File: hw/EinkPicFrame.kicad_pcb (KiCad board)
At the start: 2 copper layers, 0 parts

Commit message: HW: Created PCB
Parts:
- added C1: 100 nF, Capacitor_THT:C_Disc_D5.1mm_W3.2mm_P5.00mm, F.Cu at (115.0, 103.5)
- added C2: 0.1 uF, Capacitor_THT:C_Disc_D5.1mm_W3.2mm_P5.00mm, F.Cu at (132.2, 103.8)
- added C3: CP, Capacitor_THT:CP_Radial_D6.3mm_P2.50mm, F.Cu at (103.0, 95.8)
- added C4: 0.1 uF, Capacitor_THT:C_Disc_D5.1mm_W3.2mm_P5.00mm, F.Cu at (137.2, 89.8)
- added D1: LED, LED_THT:LED_D4.0mm, F.Cu at (103.6, 101.3)
- added J1: SD, Connector_PinSocket_2.54mm:PinSocket_1x06_P2.54mm_Vertical, F.Cu at (176.5, 103.0)
- added J2: AVR-ISP-6, Connector_PinHeader_2.54mm:PinHeader_2x03_P2.54mm_Vertical, F.Cu at (156.0, 94.0)
- added J3: EPD, Connector_PinHeader_2.54mm:PinHeader_2x04_P2.54mm_Vertical, F.Cu at (172.5, 98.0)
- added J4: Power, Connector_PinHeader_2.54mm:PinHeader_1x02_P2.54mm_Vertical, F.Cu at (105.5, 89.5)
- added J5: UART, Connector_PinSocket_2.54mm:PinSocket_1x03_P2.54mm_Vertical, F.Cu at (127.8, 103.8)
- added J6: TRIG, Connector_PinHeader_2.54mm:PinHeader_1x02_P2.54mm_Vertical, F.Cu at (111.2, 89.5)
- added Q1: 2N7000, Package_TO_SOT_THT:TO-92_Inline, F.Cu at (163.0, 103.0)
- added Q2: 2N7000, Package_TO_SOT_THT:TO-92_Inline, F.Cu at (163.0, 90.8)
- added R1: 1M, Resistor_THT:R_Axial_DIN0204_L3.6mm_D1.6mm_P2.54mm_Vertical, F.Cu at (172.5, 101.2)
- added R10: 1M, Resistor_THT:R_Axial_DIN0204_L3.6mm_D1.6mm_P2.54mm_Vertical, F.Cu at (141.2, 103.8)
- added R11: 330, Resistor_THT:R_Axial_DIN0204_L3.6mm_D1.6mm_P2.54mm_Vertical, F.Cu at (107.6, 103.5)
- added R2: 10K, Resistor_THT:R_Axial_DIN0204_L3.6mm_D1.6mm_P2.54mm_Vertical, F.Cu at (118.2, 103.0)
- added R3: 1M, Resistor_THT:R_Axial_DIN0204_L3.6mm_D1.6mm_P2.54mm_Vertical, F.Cu at (170.0, 101.2)
- added R4: 330, Resistor_THT:R_Axial_DIN0204_L3.6mm_D1.6mm_P2.54mm_Vertical, F.Cu at (162.5, 96.5)
- added R5: 330, Resistor_THT:R_Axial_DIN0204_L3.6mm_D1.6mm_P2.54mm_Vertical, F.Cu at (162.5, 94.0)
- added R6: 330, Resistor_THT:R_Axial_DIN0204_L3.6mm_D1.6mm_P2.54mm_Vertical, F.Cu at (162.5, 99.0)
- added R7: 180, Resistor_THT:R_Axial_DIN0204_L3.6mm_D1.6mm_P2.54mm_Vertical, F.Cu at (158.5, 103.0)
- added R8: 180, Resistor_THT:R_Axial_DIN0204_L3.6mm_D1.6mm_P2.54mm_Vertical, F.Cu at (158.5, 90.8)
- added R9: 1M, Resistor_THT:R_Axial_DIN0204_L3.6mm_D1.6mm_P2.54mm_Vertical, F.Cu at (148.8, 103.8)
- added REF**: KiCad-Logo2_5mm_SilkScreen, Symbol:KiCad-Logo2_5mm_SilkScreen, B.Cu at (134.7, 96.9)
- added SW1: SW_Push, Button_Switch_THT:SW_PUSH_6mm, F.Cu at (110.2, 100.0)
- added U1: ATmega328P-PU, Package_DIP:DIP-28_W7.62mm, F.Cu at (118.2, 100.5)
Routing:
- net +3V3: track 0.00 -> 232.6 mm
- net RESET: track 0.00 -> 55.3 mm
- net SDCS: track 0.00 -> 51.3 mm
- net DPCS: track 0.00 -> 31.7 mm
- net SDFET: track 0.00 -> 29.6 mm
- net LED: track 0.00 -> 26.5 mm
- net DPRST: track 0.00 -> 26.4 mm
- net DPBUSY: track 0.00 -> 25.4 mm
- net Net-(J2-Pad3): track 0.00 -> 23.9 mm
- net TRIG: track 0.00 -> 23.4 mm
- net Net-(J2-Pad1): track 0.00 -> 21.3 mm
- net DPDC: track 0.00 -> 20.5 mm
- net Net-(J2-Pad4): track 0.00 -> 17.8 mm
- net SCK: track 0.00 -> 14.5 mm
- net DPFET: track 0.00 -> 13.6 mm
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- added copper zone on B.Cu, net GND
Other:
- board outline added: 80 x 21.6 mm
- net class Power added: clearance 0.2, trace_width 0.5, via_dia 0.8, via_drill 0.4
- board text added: "(c) haJu 2022"
- board text added: "BSY"
- board text added: "CS"
- board text added: "DC"
- board text added: "EInkPicFrame 1.0"
- board text added: "GND"
- board text added: "IN"
- board text added: "ISP GND"
- board text added: "MISO"
- board text added: "MOSI"
- board text added: "RST"
- board text added: "RX"
- board text added: "Reset"
- board text added: "SCK"
- board text added: "TRIG"
- board text added: "TX"
- board text added: "VCC"

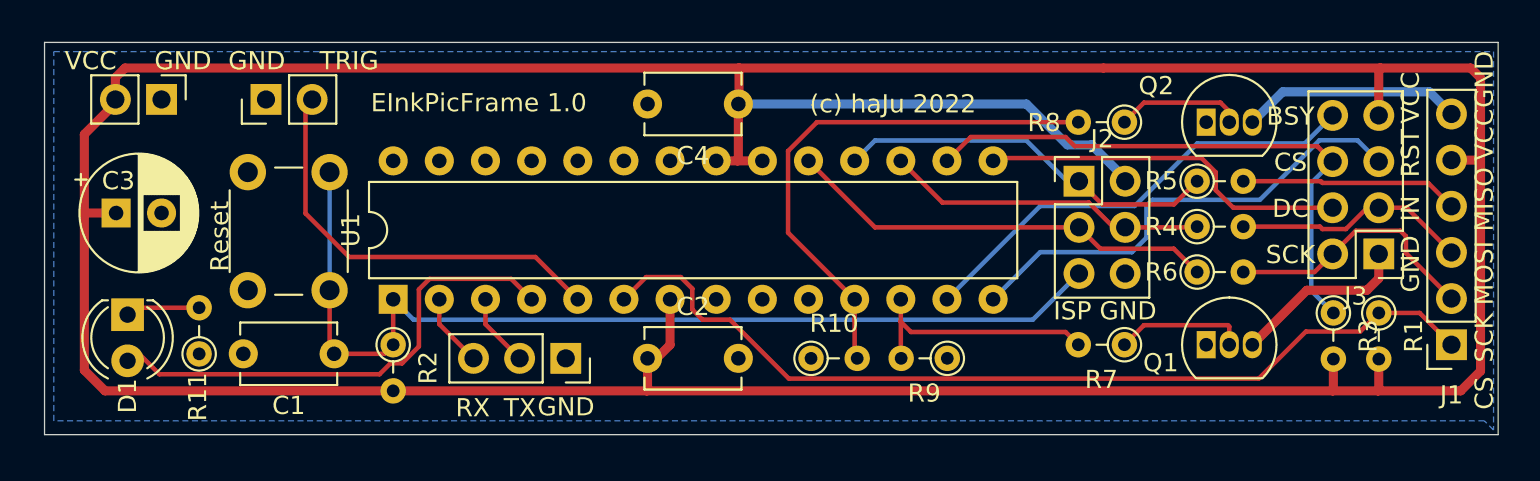
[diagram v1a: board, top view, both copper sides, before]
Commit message: HW: Added possibility to add a crystal
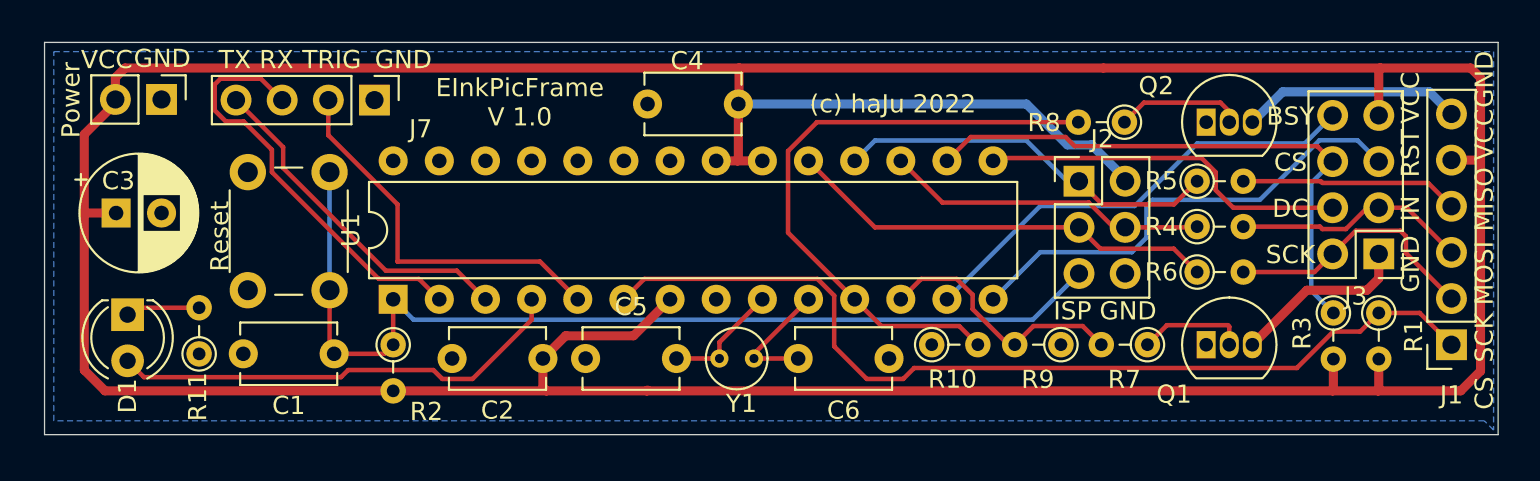
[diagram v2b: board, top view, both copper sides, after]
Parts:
- removed J5: UART, Connector_PinSocket_2.54mm:PinSocket_1x03_P2.54mm_Vertical
- removed J6: TRIG, Connector_PinHeader_2.54mm:PinHeader_1x02_P2.54mm_Vertical
- added C5: 22 pF, Capacitor_THT:C_Disc_D5.1mm_W3.2mm_P5.00mm, F.Cu at (128.8, 103.8)
- added C6: 22 pF, Capacitor_THT:C_Disc_D5.1mm_W3.2mm_P5.00mm, F.Cu at (145.5, 103.8)
- added J7: Debug, Connector_PinHeader_2.54mm:PinHeader_1x04_P2.54mm_Vertical, F.Cu at (117.2, 89.5)
- added Y1: Crystal, Crystal:Crystal_C38-LF_D3.0mm_L8.0mm_Vertical, F.Cu at (136.2, 103.8)
- moved R10 6.68 mm to (147.9, 103.0)
- moved R9 6.30 mm to (155.0, 103.0)
- moved C2 5.76 mm to (126.5, 103.8), turned to 180 degrees
- moved R7 1.27 mm to (159.8, 103.0)
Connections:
- U1 pad 10: Net-(U1-Pad10) -> XTAL2
- U1 pad 9: Net-(U1-Pad9) -> XTAL1
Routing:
- net RXD: track 4.03 -> 23.1 mm
- net TXD: track 4.03 -> 18.9 mm
- net XTAL2: track 0.00 -> 7.25 mm
- net XTAL1: track 0.00 -> 6.60 mm
- net SDFET: track 29.6 -> 34.1 mm
- net +3V3: track 232.6 -> 237.0 mm
- net TRIG: track 23.4 -> 21.2 mm
- net Net-(Q1-Pad2): track 7.25 -> 5.98 mm
- net LED: track 26.5 -> 25.5 mm
- net SDCS: track 51.3 -> 52.2 mm
- net DPFET: track 13.6 -> 14.3 mm
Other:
- board text added: "EInkPicFrame V 1.0"
- board text added: "Power"
- board text removed: "EInkPicFrame 1.0"

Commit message: HW: ADC + Small improvements (V1.1)
Added proper wiring for AVCC and AREF according to data sheet
 * 100 nF capacitor to ground on AREF
 *  10 uH inductor on AVCC

 Added header for unused PortC pins
  * May be used as 2nd SPI (bit bang)
  * Independent SPI would allow to power EPD and SD independently

Use larger footprint for the FET transistors for easier soldering

Add a jumper to disconnect VCC without pulling battery connector
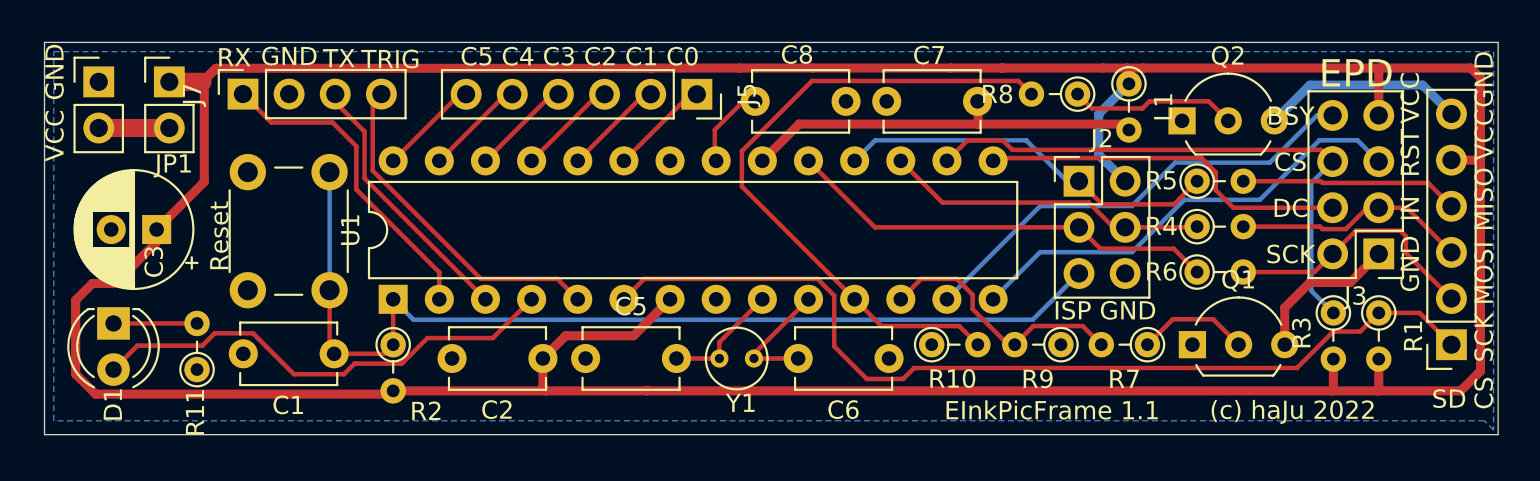
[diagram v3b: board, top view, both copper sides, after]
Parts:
- removed C4: 0.1 uF, Capacitor_THT:C_Disc_D5.1mm_W3.2mm_P5.00mm
- added C7: 0.1 uF, Capacitor_THT:C_Disc_D5.1mm_W3.2mm_P5.00mm, F.Cu at (145.4, 89.6)
- added C8: 0.1 uF, Capacitor_THT:C_Disc_D5.1mm_W3.2mm_P5.00mm, F.Cu at (138.2, 89.6)
- added J5: PORTC, Connector_PinSocket_2.54mm:PinSocket_1x06_P2.54mm_Vertical, F.Cu at (135.0, 89.2)
- added JP1: Jumper, Connector_PinHeader_2.54mm:PinHeader_1x02_P2.54mm_Vertical, F.Cu at (105.9, 88.5)
- added L1: 10 uH, Resistor_THT:R_Axial_DIN0204_L3.6mm_D1.6mm_P2.54mm_Vertical, F.Cu at (158.7, 88.6)
- J7: footprint Connector_PinHeader_2.54mm:PinHeader_1x04_P2.54mm_Vertical -> Connector_PinSocket_2.54mm:PinSocket_1x04_P2.54mm_Vertical
- Q1: footprint Package_TO_SOT_THT:TO-92_Inline -> Package_TO_SOT_THT:TO-92L_Inline_Wide
- Q2: footprint Package_TO_SOT_THT:TO-92_Inline -> Package_TO_SOT_THT:TO-92_Inline_Wide
- moved J7 7.25 mm to (110.0, 89.2), turned to 90 degrees
- moved J4 3.59 mm to (102.0, 88.5), turned to 0 degrees
- moved R8 3.00 mm to (155.9, 89.2)
- moved C3 2.41 mm to (105.2, 96.7), turned to 180 degrees
- moved Q2 1.33 mm to (161.7, 90.7)
- moved D1 0.91 mm to (102.9, 101.8)
- moved R11 0.87 mm to (107.5, 104.4)
- moved Q1 0.76 mm to (162.2, 103.0)
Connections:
- J4 pad 2: +3V3 -> Net-(J4-Pad2)
- J7 pad 1: GND -> RXD
- J7 pad 2: TRIG -> GND
- J7 pad 3: RXD -> TXD
- J7 pad 4: TXD -> TRIG
- U1 pad 20: +3V3 -> Net-(C7-Pad2)
- U1 pad 21: +3V3 -> Net-(C8-Pad1)
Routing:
- net Net-(C7-Pad2): track 0.00 -> 22.4 mm
- net +3V3: track 237.0 -> 215.1 mm
- net Net-(J5-Pad2): track 0.00 -> 5.53 mm
- net Net-(J5-Pad1): track 0.00 -> 5.53 mm
- net Net-(J5-Pad5): track 0.00 -> 5.53 mm
- net Net-(J5-Pad4): track 0.00 -> 5.53 mm
- net Net-(J5-Pad3): track 0.00 -> 5.53 mm
- net RXD: track 23.1 -> 17.7 mm
- net Net-(J5-Pad6): track 0.00 -> 5.10 mm
- net Net-(C8-Pad1): track 0.00 -> 4.54 mm
- net TXD: track 18.9 -> 14.9 mm
- net Net-(J4-Pad2): track 0.00 -> 3.89 mm
- net TRIG: track 21.2 -> 18.4 mm
- net SDFET: track 34.1 -> 36.4 mm
- net Net-(Q2-Pad2): track 7.01 -> 9.22 mm
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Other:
- board text added: "C5 C4 C3 C2 C1 C0"
- board text added: "EInkPicFrame 1.1"
- board text added: "EPD"
- board text added: "SD"
- board text added: "https://github.com/nhjschulz/EInkPicFrame"
- board text removed: "EInkPicFrame V 1.0"
- board text removed: "Power"
